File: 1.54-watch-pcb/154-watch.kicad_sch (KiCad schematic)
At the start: 60 parts, among them J1 AFC24-S24FIC-00, J2 Conn_01x06_Female, J3 USB_C_Programming, J4 Jack-DC, J5 Conn_01x02_Male, Q1 Si1308, Q2 BC817, Q3 BC817, Q4 Si2301CDS, SW1 RESET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

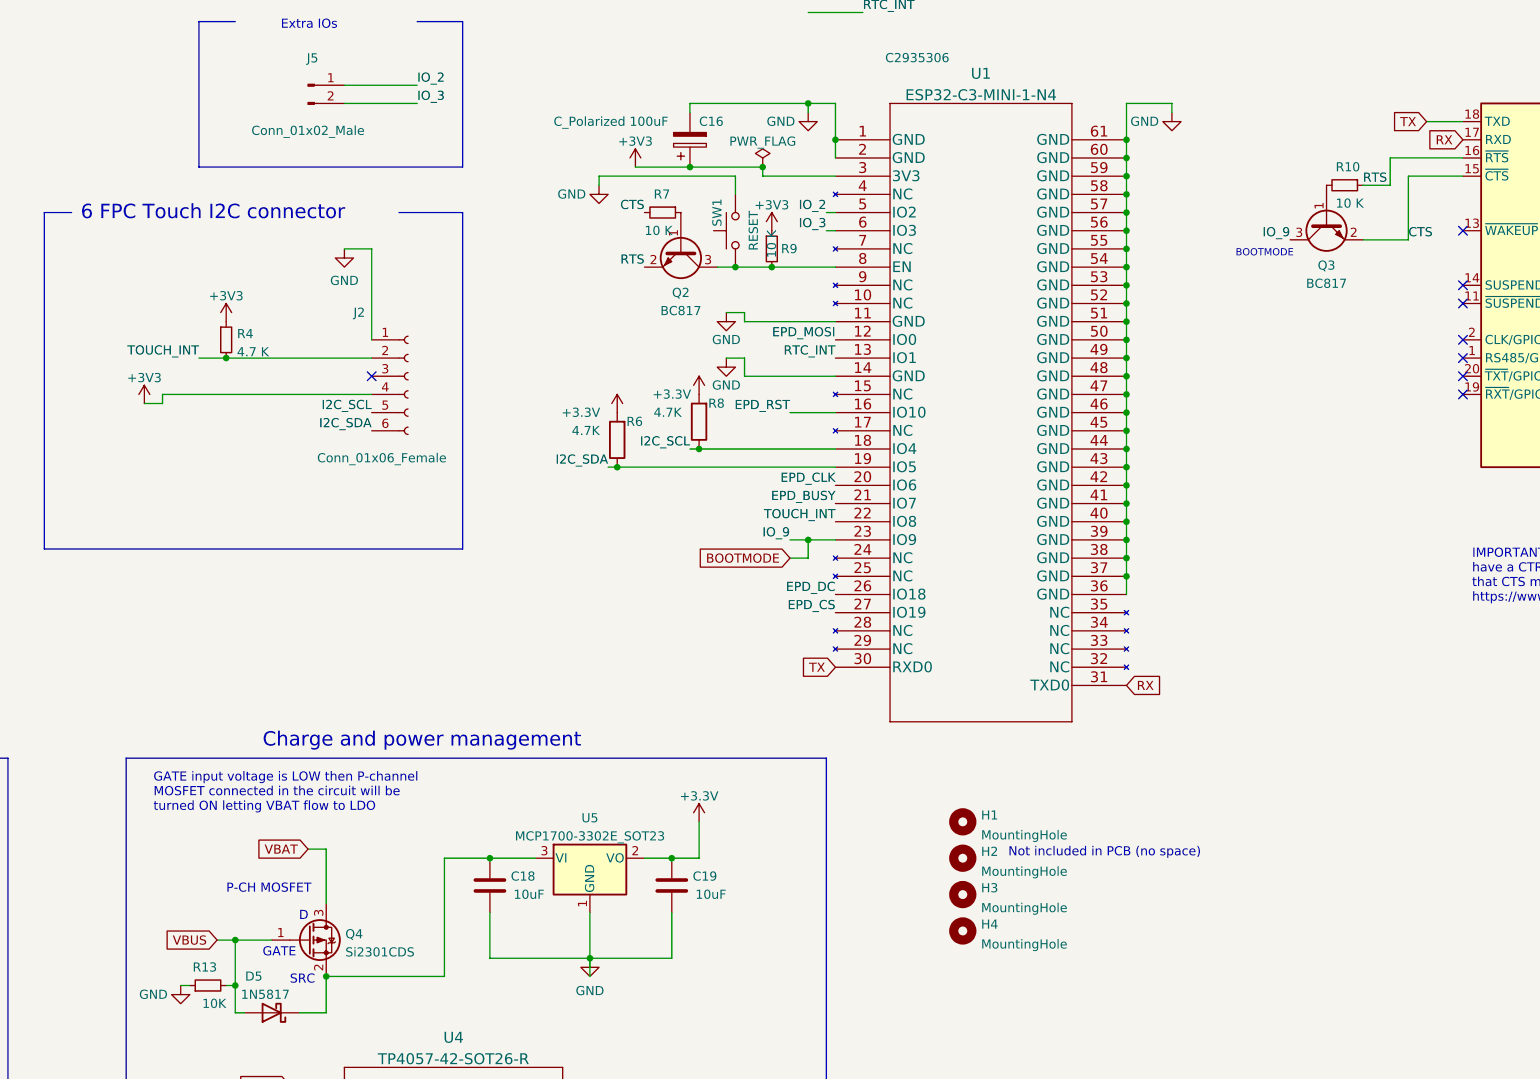
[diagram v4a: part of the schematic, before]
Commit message: Add some test points in case UART works incorrectly https://github.com/martinberlin/H-spi-adapters/issues/9
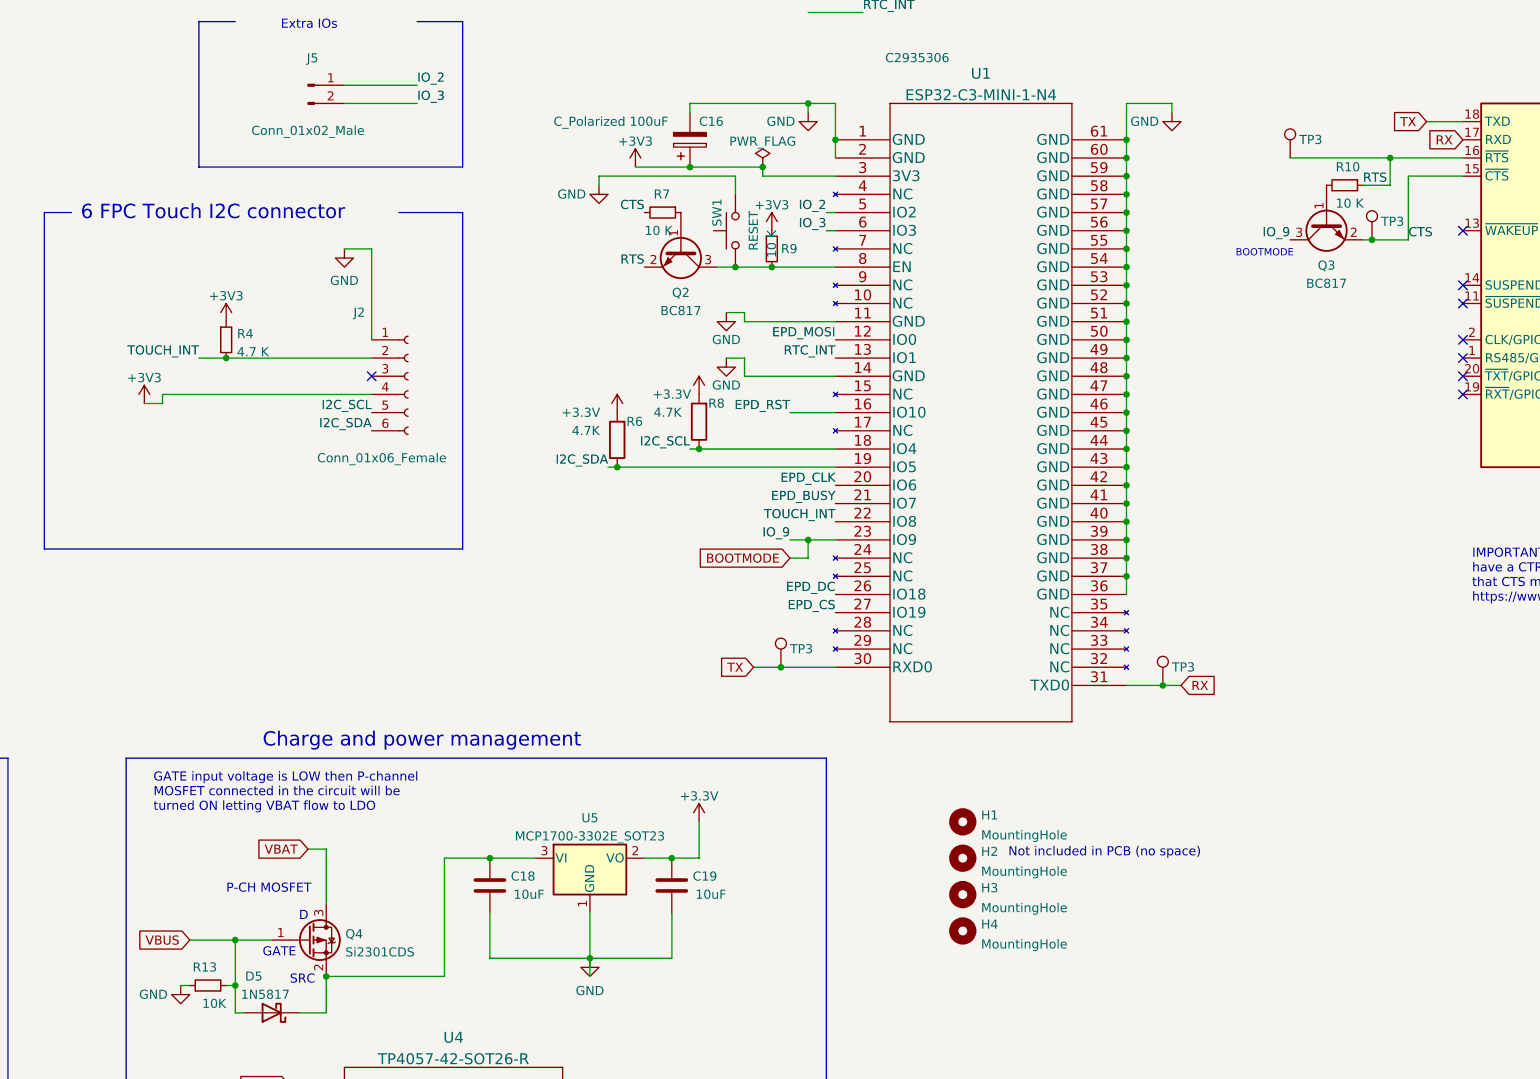
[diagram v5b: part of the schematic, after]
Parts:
- added TP3 (x4): 32Khz, TestPoint:TestPoint_Pad_1.0x1.0mm, symbol Connector:TestPoint
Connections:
- net CTS: now also TP3.1
- net RTS: now also TP3.1
- net RX: now also TP3.1
- net TX: now also TP3.1
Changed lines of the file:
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@@
   (junction (at 99.06 114.3) (diameter 0) (color 0 0 0 0)
   )
+  (junction (at 287.02 143.51) (diameter 0) (color 0 0 0 0)
+  )
   (junction (at 281.94 128.27) (diameter 0) (color 0 0 0 0)
   )
+  (junction (at 318.77 69.85) (diameter 0) (color 0 0 0 0)
+  )
   (junction (at 82.55 57.15) (diameter 0) (color 0 0 0 0)
   )
@@
   (junction (at 67.31 167.64) (diameter 0) (color 0 0 0 0)
   )
+  (junction (at 316.23 81.28) (diameter 0) (color 0 0 0 0)
+  )
   (junction (at 281.94 105.41) (diameter 0) (color 0 0 0 0)
   )
@@
   (junction (at 207.01 181.61) (diameter 0) (color 0 0 0 0)
   )
+  (junction (at 233.68 140.97) (diameter 0) (color 0 0 0 0)
+  )
   (junction (at 106.68 114.3) (diameter 0) (color 0 0 0 0)
   )
@@
     (stroke (width 0) (type default))
   )
+  (wire (pts (xy 233.68 140.97) (xy 241.3 140.97))
+    (stroke (width 0) (type default))
+  )
   (wire (pts (xy 281.94 123.19) (xy 281.94 120.65))
     (stroke (width 0) (type default))
@@
     (stroke (width 0) (type default))
   )
+  (wire (pts (xy 229.87 140.97) (xy 233.68 140.97))
+    (stroke (width 0) (type default))
+  )
   (wire (pts (xy 229.87 214.63) (xy 229.87 200.66))
     (stroke (width 0) (type default))
@@
     (stroke (width 0) (type default))
   )
+  (wire (pts (xy 151.13 179.07) (xy 157.48 179.07))
+    (stroke (width 0) (type default))
+  )
   (wire (pts (xy 224.79 204.47) (xy 224.79 205.74))
     (stroke (width 0) (type default))
@@
     (stroke (width 0) (type default))
   )
+  (wire (pts (xy 289.56 143.51) (xy 287.02 143.51))
+    (stroke (width 0) (type default))
+  )
   (wire (pts (xy 207.01 181.61) (xy 218.44 181.61))
     (stroke (width 0) (type default))
@@
     (stroke (width 0) (type default))
   )
+  (wire (pts (xy 316.23 81.28) (xy 314.96 81.28))
+    (stroke (width 0) (type default))
+  )
   (wire (pts (xy 170.18 166.37) (xy 170.18 173.99))
     (stroke (width 0) (type default))
@@
     (stroke (width 0) (type default))
   )
-  (wire (pts (xy 154.94 179.07) (xy 157.48 179.07))
-    (stroke (width 0) (type default))
-  )
   (wire (pts (xy 241.3 92.71) (xy 228.6 92.71))
     (stroke (width 0) (type default))
@@
     (stroke (width 0) (type default))
   )
+  (wire (pts (xy 287.02 143.51) (xy 281.94 143.51))
+    (stroke (width 0) (type default))
+  )
   (wire (pts (xy 172.72 82.55) (xy 176.53 82.55))
     (stroke (width 0) (type default))
@@
     (stroke (width 0) (type default))
   )
+  (wire (pts (xy 304.8 69.85) (xy 318.77 69.85))
+    (stroke (width 0) (type default))
+  )
   (wire (pts (xy 58.42 96.52) (xy 62.23 96.52))
     (stroke (width 0) (type default))
@@
     (stroke (width 0) (type default))
   )
-  (wire (pts (xy 321.31 81.28) (xy 314.96 81.28))
+  (wire (pts (xy 321.31 81.28) (xy 316.23 81.28))
     (stroke (width 0) (type default))
   )
@@
     )
   )
-  (global_label "TX" (shape input) (at 241.3 140.97 180) (fields_autoplaced)
+  (global_label "TX" (shape input) (at 229.87 140.97 180) (fields_autoplaced)
     (effects (font (size 1.27 1.27)) (justify right))
-    (property "Intersheetrefs" "${INTERSHEET_REFS}" (at 236.7098 141.0494 0)
+    (property "Intersheetrefs" "${INTERSHEET_REFS}" (at 225.2798 141.0494 0)
       (effects (font (size 1.27 1.27)) (justify right) hide)
     )
@@
     )
   )
-  (global_label "RX" (shape input) (at 281.94 143.51 0) (fields_autoplaced)
+  (global_label "RX" (shape input) (at 289.56 143.51 0) (fields_autoplaced)
     (effects (font (size 1.27 1.27)) (justify left))
-    (property "Intersheetrefs" "${INTERSHEET_REFS}" (at 286.8326 143.4306 0)
+    (property "Intersheetrefs" "${INTERSHEET_REFS}" (at 294.4526 143.4306 0)
       (effects (font (size 1.27 1.27)) (justify left) hide)
     )
   )
-  (global_label "VBUS" (shape input) (at 154.94 179.07 180) (fields_autoplaced)
+  (global_label "VBUS" (shape input) (at 151.13 179.07 180) (fields_autoplaced)
     (effects (font (size 1.27 1.27)) (justify right))
-    (property "Intersheetrefs" "${INTERSHEET_REFS}" (at 147.6283 178.9906 0)
+    (property "Intersheetrefs" "${INTERSHEET_REFS}" (at 143.8183 178.9906 0)
       (effects (font (size 1.27 1.27)) (justify right) hide)
     )
@@
     )
   )
+  (symbol (lib_id "Connector:TestPoint") (at 287.02 143.51 0) (mirror y) (unit 1)
+    (in_bom yes) (on_board yes) (dnp no)
+    (property "Reference" "TP3" (at 288.29 140.97 0)
+      (effects (font (size 1.27 1.27)) (justify right))
+    )
+    (property "Value" "32Khz" (at 288.417 141.9102 0)
+      (effects (font (size 1.27 1.27)) (justify right) hide)
+    )
+    (property "Footprint" "TestPoint:TestPoint_Pad_1.0x1.0mm" (at 283.21 147.32 0)
+      (effects (font (size 1.27 1.27)) hide)
+    )
+    (property "Datasheet" "~" (at 281.94 143.51 0)
+      (effects (font (size 1.27 1.27)) hide)
+    )
+    (pin "1")
+    (instances
+      (project "C3-27-epaper-touch"
+        (path "/42575459-fa0a-4761-8328-0238c17cbdda"
+          (reference "TP3") (unit 1)
+        )
+      )
+      (project "154-watch"
+        (path "/ea6fde00-59dc-4a79-a647-7e38199fae0e"
+          (reference "TP4") (unit 1)
+        )
+      )
+    )
+  )
   (symbol (lib_id "power:+3.3V") (at 105.41 173.99 0) (unit 1)
     (in_bom yes) (on_board yes) (dnp no)
@@
     )
   )
+  (symbol (lib_id "Connector:TestPoint") (at 233.68 140.97 0) (mirror y) (unit 1)
+    (in_bom yes) (on_board yes) (dnp no)
+    (property "Reference" "TP3" (at 234.95 138.43 0)
+      (effects (font (size 1.27 1.27)) (justify right))
+    )
+    (property "Value" "32Khz" (at 235.077 139.3702 0)
+      (effects (font (size 1.27 1.27)) (justify right) hide)
+    )
+    (property "Footprint" "TestPoint:TestPoint_Pad_1.0x1.0mm" (at 229.87 144.78 0)
+      (effects (font (size 1.27 1.27)) hide)
+    )
+    (property "Datasheet" "~" (at 228.6 140.97 0)
+      (effects (font (size 1.27 1.27)) hide)
+    )
+    (pin "1")
+    (instances
+      (project "C3-27-epaper-touch"
+        (path "/42575459-fa0a-4761-8328-0238c17cbdda"
+          (reference "TP3") (unit 1)
+        )
+      )
+      (project "154-watch"
+        (path "/ea6fde00-59dc-4a79-a647-7e38199fae0e"
+          (reference "TP3") (unit 1)
+        )
+      )
+    )
+  )
   (symbol (lib_id "Device:C") (at 64.77 176.53 90) (unit 1)
     (in_bom yes) (on_board yes) (dnp no)
@@
     )
   )
+  (symbol (lib_id "Connector:TestPoint") (at 316.23 81.28 0) (mirror y) (unit 1)
+    (in_bom yes) (on_board yes) (dnp no)
+    (property "Reference" "TP3" (at 317.5 78.74 0)
+      (effects (font (size 1.27 1.27)) (justify right))
+    )
+    (property "Value" "32Khz" (at 317.627 79.6802 0)
+      (effects (font (size 1.27 1.27)) (justify right) hide)
+    )
+    (property "Footprint" "TestPoint:TestPoint_Pad_1.0x1.0mm" (at 312.42 85.09 0)
+      (effects (font (size 1.27 1.27)) hide)
+    )
+    (property "Datasheet" "~" (at 311.15 81.28 0)
+      (effects (font (size 1.27 1.27)) hide)
+    )
+    (pin "1")
+    (instances
+      (project "C3-27-epaper-touch"
+        (path "/42575459-fa0a-4761-8328-0238c17cbdda"
+          (reference "TP3") (unit 1)
+        )
+      )
+      (project "154-watch"
+        (path "/ea6fde00-59dc-4a79-a647-7e38199fae0e"
+          (reference "TP2") (unit 1)
+        )
+      )
+    )
+  )
   (symbol (lib_id "power:PWR_FLAG") (at 231.14 71.12 0) (unit 1)
     (in_bom yes) (on_board yes) (dnp no) (fields_autoplaced)
@@
         )
       )
+    )
+  )
+  (symbol (lib_id "Connector:TestPoint") (at 304.8 69.85 0) (mirror y) (unit 1)
+    (in_bom yes) (on_board yes) (dnp no)
+    (property "Reference" "TP3" (at 306.07 67.31 0)
+      (effects (font (size 1.27 1.27)) (justify right))
+    )
+    (property "Value" "32Khz" (at 306.197 68.2502 0)
+      (effects (font (size 1.27 1.27)) (justify right) hide)
+    )
+    (property "Footprint" "TestPoint:TestPoint_Pad_1.0x1.0mm" (at 300.99 73.66 0)
+      (effects (font (size 1.27 1.27)) hide)
+    )
+    (property "Datasheet" "~" (at 299.72 69.85 0)
+      (effects (font (size 1.27 1.27)) hide)
+    )
+    (pin "1")
+    (instances
+      (project "C3-27-epaper-touch"
+        (path "/42575459-fa0a-4761-8328-0238c17cbdda"
+          (reference "TP3") (unit 1)
+        )
+      )
+      (project "154-watch"
+        (path "/ea6fde00-59dc-4a79-a647-7e38199fae0e"
+          (reference "TP1") (unit 1)
+        )
+      )
